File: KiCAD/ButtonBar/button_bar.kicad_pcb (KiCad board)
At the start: 2 copper layers, 14 parts, among them P1 Buttons, SW1 SW_UP, SW2 SW_DN, SW3 SW_OK, SW4 SW_LT, SW5 SW_RT, SW6 RESET

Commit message: redo tracks
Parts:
- moved R1 11.4 mm to (219.2, 85.6)
- moved R2 10.4 mm to (198.3, 58.9), turned to 180 degrees
- moved R4 5.86 mm to (198.0, 85.6), turned to 0 degrees
- moved R10 5.32 mm to (219.8, 58.8)
- moved R3 1.24 mm to (208.7, 85.6)
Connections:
- C1 pad 1: /RST -> GND
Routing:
- net /SW: track 118.9 -> 0.00 mm, vias 1 -> 0
- net /PWR: track 94.8 -> 0.00 mm
- net GND: track 73.3 -> 0.00 mm
- net N-000004: track 46.9 -> 0.00 mm
- net N-000002: track 43.0 -> 0.00 mm
- net N-000003: track 38.8 -> 0.00 mm
- net /RST: track 27.5 -> 0.00 mm
- net N-000001: track 17.8 -> 0.00 mm
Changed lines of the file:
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@@
   (general
     (links 34)
-    (no_connects 12)
-    (area 186.093599 35.6362 232.9942 120.4214)
+    (no_connects 34)
+    (area 0 0 0 0)
     (thickness 1.6)
     (drawings 0)
-    (tracks 64)
+    (tracks 0)
     (zones 0)
     (modules 14)
@@
     (pad 1 thru_hole circle (at 2.54 0 90) (size 1.524 1.524) (drill 0.889)
       (layers *.Cu *.Mask F.SilkS)
-      (net 2 /RST)
+      (net 4 GND)
     )
     (model "uControl_Libs/3D Modules/capa_2pas_5x5mm.wrl"
@@
   )
   (module RC03 (layer F.Cu)
-    (at 228.1682 92.583 180)
+    (at 219.1512 85.5726 180)
     (descr "Resistor, RC03")
     (tags R)
@@
   )
   (module RC03 (layer F.Cu)
-    (at 191.8462 50.8 90)
+    (at 198.3486 58.9407 180)
     (descr "Resistor, RC03")
     (tags R)
     (autoplace_cost180 10)
-    (fp_text reference R2 (at 0 0 90) (layer F.SilkS)
+    (fp_text reference R2 (at 0 0 180) (layer F.SilkS)
       (effects (font (size 1.016 1.016) (thickness 0.127)))
     )
-    (fp_text value 10K (at 0 1.9685 90) (layer F.SilkS)
+    (fp_text value 10K (at 0 1.9685 180) (layer F.SilkS)
       (effects (font (size 1.27 1.27) (thickness 0.1524)))
     )
@@
     (fp_line (start 2.159 0.889) (end 2.159 -0.889) (layer F.SilkS) (width 0.254))
     (fp_line (start 2.159 -0.889) (end -2.159 -0.889) (layer F.SilkS) (width 0.254))
-    (pad 2 thru_hole circle (at -3.81 0 90) (size 1.524 1.524) (drill 0.889)
+    (pad 2 thru_hole circle (at -3.81 0 180) (size 1.524 1.524) (drill 0.889)
       (layers *.Cu *.Mask F.SilkS)
       (net 8 N-000004)
     )
-    (pad 1 thru_hole circle (at 3.81 0 90) (size 1.524 1.524) (drill 0.889)
+    (pad 1 thru_hole circle (at 3.81 0 180) (size 1.524 1.524) (drill 0.889)
       (layers *.Cu *.Mask F.SilkS)
       (net 1 /PWR)
@@
   )
   (module RC03 (layer F.Cu)
-    (at 209.931 85.9536 180)
+    (at 208.7372 85.6234 180)
     (descr "Resistor, RC03")
     (tags R)
@@
   )
   (module RC03 (layer F.Cu)
-    (at 192.2526 86.5632 270)
+    (at 198.0438 85.6488)
     (descr "Resistor, RC03")
     (tags R)
     (autoplace_cost180 10)
-    (fp_text reference R4 (at 0 0 270) (layer F.SilkS)
+    (fp_text reference R4 (at -0.6096 -0.4572) (layer F.SilkS)
       (effects (font (size 1.016 1.016) (thickness 0.127)))
     )
-    (fp_text value 10K (at 0 1.9685 270) (layer F.SilkS)
+    (fp_text value 10K (at 0 1.9685) (layer F.SilkS)
       (effects (font (size 1.27 1.27) (thickness 0.1524)))
     )
@@
     (fp_line (start 2.159 0.889) (end 2.159 -0.889) (layer F.SilkS) (width 0.254))
     (fp_line (start 2.159 -0.889) (end -2.159 -0.889) (layer F.SilkS) (width 0.254))
-    (pad 2 thru_hole circle (at -3.81 0 270) (size 1.524 1.524) (drill 0.889)
+    (pad 2 thru_hole circle (at -3.81 0) (size 1.524 1.524) (drill 0.889)
       (layers *.Cu *.Mask F.SilkS)
       (net 6 N-000002)
     )
-    (pad 1 thru_hole circle (at 3.81 0 270) (size 1.524 1.524) (drill 0.889)
+    (pad 1 thru_hole circle (at 3.81 0) (size 1.524 1.524) (drill 0.889)
       (layers *.Cu *.Mask F.SilkS)
       (net 7 N-000003)
@@
   )
   (module RC03 (layer F.Cu)
-    (at 225.1202 58.801 180)
+    (at 219.7989 58.7883 180)
     (descr "Resistor, RC03")
     (tags R)
@@
     )
   )
-  (segment (start 191.8462 46.99) (end 204.9874 46.99) (width 0.254) (layer B.Cu) (net 1) (status 400000))
-  (segment (start 204.9874 46.99) (end 206.8682 45.1092) (width 0.254) (layer B.Cu) (net 1) (status 800000))
-  (segment (start 206.8682 45.1092) (end 206.8682 49.0326) (width 0.254) (layer F.Cu) (net 1))
-  (segment (start 219.6596 107.29) (end 222.9 107.29) (width 0.254) (layer F.Cu) (net 1))
-  (segment (start 217.9066 105.537) (end 219.6596 107.29) (width 0.254) (layer F.Cu) (net 1))
-  (segment (start 217.9066 60.071) (end 217.9066 105.537) (width 0.254) (layer F.Cu) (net 1))
-  (segment (start 206.8682 49.0326) (end 217.9066 60.071) (width 0.254) (layer F.Cu) (net 1))
-  (segment (start 230.6574 108.6612) (end 224.2712 108.6612) (width 0.254) (layer F.Cu) (net 1))
-  (segment (start 224.2712 108.6612) (end 222.9 107.29) (width 0.254) (layer F.Cu) (net 1))
-  (segment (start 230.6574 101.0412) (end 224.0688 101.0412) (width 0.254) (layer B.Cu) (net 2))
-  (segment (start 224.0688 101.0412) (end 222.9 102.21) (width 0.254) (layer B.Cu) (net 2))
-  (segment (start 222.9 102.21) (end 216.013 102.21) (width 0.254) (layer B.Cu) (net 2))
-  (segment (start 216.013 102.21) (end 207.2746 110.9484) (width 0.254) (layer B.Cu) (net 2))
-  (segment (start 192.6738 73.354) (end 195.378 73.354) (width 0.254) (layer F.Cu) (net 3) (status 400000))
-  (segment (start 203.918 64.814) (end 209.125 64.814) (width 0.254) (layer B.Cu) (net 3))
-  (segment (start 202.6158 66.1162) (end 203.918 64.814) (width 0.254) (layer B.Cu) (net 3))
-  (via (at 202.6158 66.1162) (size 0.889) (layers F.Cu B.Cu) (net 3))
-  (segment (start 195.378 73.354) (end 202.6158 66.1162) (width 0.254) (layer F.Cu) (net 3))
-  (segment (start 229.0466 73.354) (end 229.0466 77.1504) (width 0.254) (layer B.Cu) (net 3) (status 400000))
-  (segment (start 224.3582 81.8388) (end 224.3582 92.583) (width 0.254) (layer B.Cu) (net 3) (status 800000))
-  (segment (start 229.0466 77.1504) (end 224.3582 81.8388) (width 0.254) (layer B.Cu) (net 3))
-  (segment (start 211.165 73.354) (end 211.165 81.5192) (width 0.254) (layer B.Cu) (net 3) (status 400000))
-  (segment (start 209.6516 94.195) (end 210.9618 95.5052) (width 0.254) (layer B.Cu) (net 3) (status 800000))
-  (segment (start 209.6516 83.0326) (end 209.6516 94.195) (width 0.254) (layer B.Cu) (net 3))
-  (segment (start 211.165 81.5192) (end 209.6516 83.0326) (width 0.254) (layer B.Cu) (net 3))
-  (segment (start 211.3682 45.1092) (end 211.3682 55.0524) (width 0.254) (layer B.Cu) (net 3) (status 400000))
-  (segment (start 208.8896 64.5786) (end 209.125 64.814) (width 0.254) (layer B.Cu) (net 3))
-  (segment (start 209.125 64.814) (end 211.165 66.854) (width 0.254) (layer B.Cu) (net 3) (status 800000))
-  (segment (start 208.8896 57.531) (end 208.8896 64.5786) (width 0.254) (layer B.Cu) (net 3))
-  (segment (start 211.3682 55.0524) (end 208.8896 57.531) (width 0.254) (layer B.Cu) (net 3))
-  (segment (start 224.3582 92.583) (end 224.3582 99.822) (width 0.254) (layer F.Cu) (net 3))
-  (segment (start 224.3582 99.822) (end 230.6574 106.1212) (width 0.254) (layer F.Cu) (net 3))
-  (segment (start 224.3582 92.583) (end 213.884 92.583) (width 0.254) (layer B.Cu) (net 3))
-  (segment (start 213.884 92.583) (end 210.9618 95.5052) (width 0.254) (layer B.Cu) (net 3))
-  (segment (start 231.9782 92.583) (end 231.9782 61.849) (width 0.254) (layer B.Cu) (net 4) (status 400000))
-  (segment (start 231.9782 61.849) (end 228.9302 58.801) (width 0.254) (layer B.Cu) (net 4) (status 800000))
-  (segment (start 230.6574 103.5812) (end 232.4862 103.5812) (width 0.254) (layer B.Cu) (net 4) (status 400000))
-  (segment (start 233.0958 93.7006) (end 231.9782 92.583) (width 0.254) (layer B.Cu) (net 4) (status 800000))
-  (segment (start 233.0958 102.9716) (end 233.0958 93.7006) (width 0.254) (layer B.Cu) (net 4))
-  (segment (start 232.4862 103.5812) (end 233.0958 102.9716) (width 0.254) (layer B.Cu) (net 4))
-  (segment (start 230.6574 103.5812) (end 230.6574 103.7082) (width 0.254) (layer B.Cu) (net 4))
-  (segment (start 216.9172 117.4484) (end 211.7746 117.4484) (width 0.254) (layer B.Cu) (net 4))
-  (segment (start 230.6574 103.7082) (end 216.9172 117.4484) (width 0.254) (layer B.Cu) (net 4))
-  (segment (start 221.3102 58.801) (end 221.3102 63.6176) (width 0.254) (layer B.Cu) (net 5) (status 400000))
-  (segment (start 221.3102 63.6176) (end 224.5466 66.854) (width 0.254) (layer B.Cu) (net 5) (status 800000))
-  (segment (start 212.9282 58.928) (end 221.1832 58.928) (width 0.254) (layer B.Cu) (net 5) (status C00000))
-  (segment (start 221.1832 58.928) (end 221.3102 58.801) (width 0.254) (layer B.Cu) (net 5) (status C00000))
-  (segment (start 188.1738 73.354) (end 188.1738 78.6744) (width 0.254) (layer B.Cu) (net 6) (status 400000))
-  (segment (start 188.1738 78.6744) (end 192.2526 82.7532) (width 0.254) (layer B.Cu) (net 6) (status 800000))
-  (segment (start 205.3082 58.928) (end 195.326 58.928) (width 0.254) (layer F.Cu) (net 6) (status 400000))
-  (segment (start 188.1738 66.0802) (end 188.1738 66.854) (width 0.254) (layer F.Cu) (net 6) (status C00000))
-  (segment (start 195.326 58.928) (end 188.1738 66.0802) (width 0.254) (layer F.Cu) (net 6) (status 800000))
-  (segment (start 188.1738 73.354) (end 188.1738 77.5822) (width 0.254) (layer B.Cu) (net 6) (status 400000))
-  (segment (start 188.1738 77.5822) (end 192.9638 82.3722) (width 0.254) (layer B.Cu) (net 6))
-  (segment (start 213.741 85.9536) (end 213.741 80.43) (width 0.254) (layer F.Cu) (net 7) (status 400000))
-  (segment (start 213.741 80.43) (end 206.665 73.354) (width 0.254) (layer F.Cu) (net 7) (status 800000))
-  (segment (start 192.2526 90.3732) (end 209.3214 90.3732) (width 0.254) (layer F.Cu) (net 7) (status 400000))
-  (segment (start 209.3214 90.3732) (end 213.741 85.9536) (width 0.254) (layer F.Cu) (net 7) (status 800000))
-  (segment (start 206.121 85.9536) (end 206.121 82.55) (width 0.254) (layer B.Cu) (net 8) (status 400000))
-  (segment (start 198.9582 61.722) (end 191.8462 54.61) (width 0.254) (layer B.Cu) (net 8) (status 800000))
-  (segment (start 198.9582 75.3872) (end 198.9582 61.722) (width 0.254) (layer B.Cu) (net 8))
-  (segment (start 206.121 82.55) (end 198.9582 75.3872) (width 0.254) (layer B.Cu) (net 8))
-  (segment (start 206.4618 95.5052) (end 206.4618 86.2944) (width 0.254) (layer B.Cu) (net 8))
-  (segment (start 206.4618 86.2944) (end 206.121 85.9536) (width 0.254) (layer B.Cu) (net 8))
 )

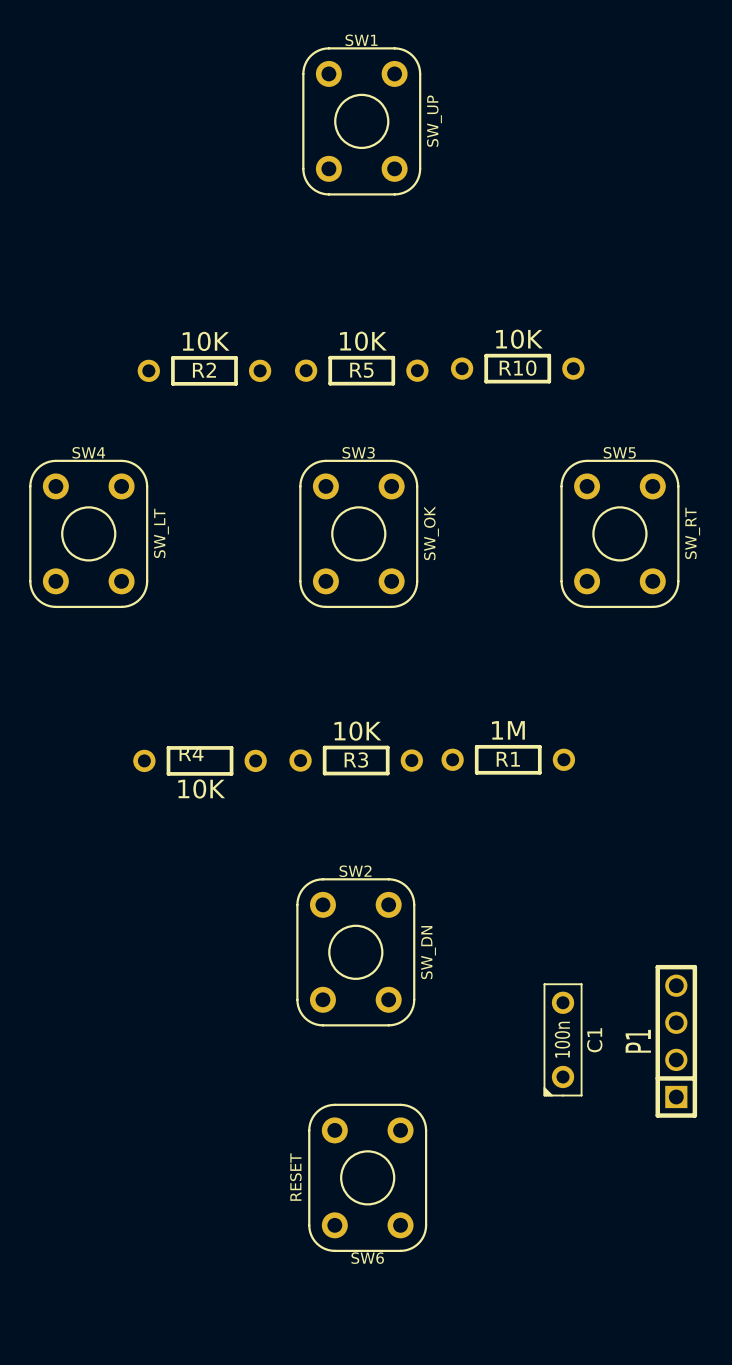
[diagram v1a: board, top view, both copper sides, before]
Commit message: finished tracks on ButtonBar
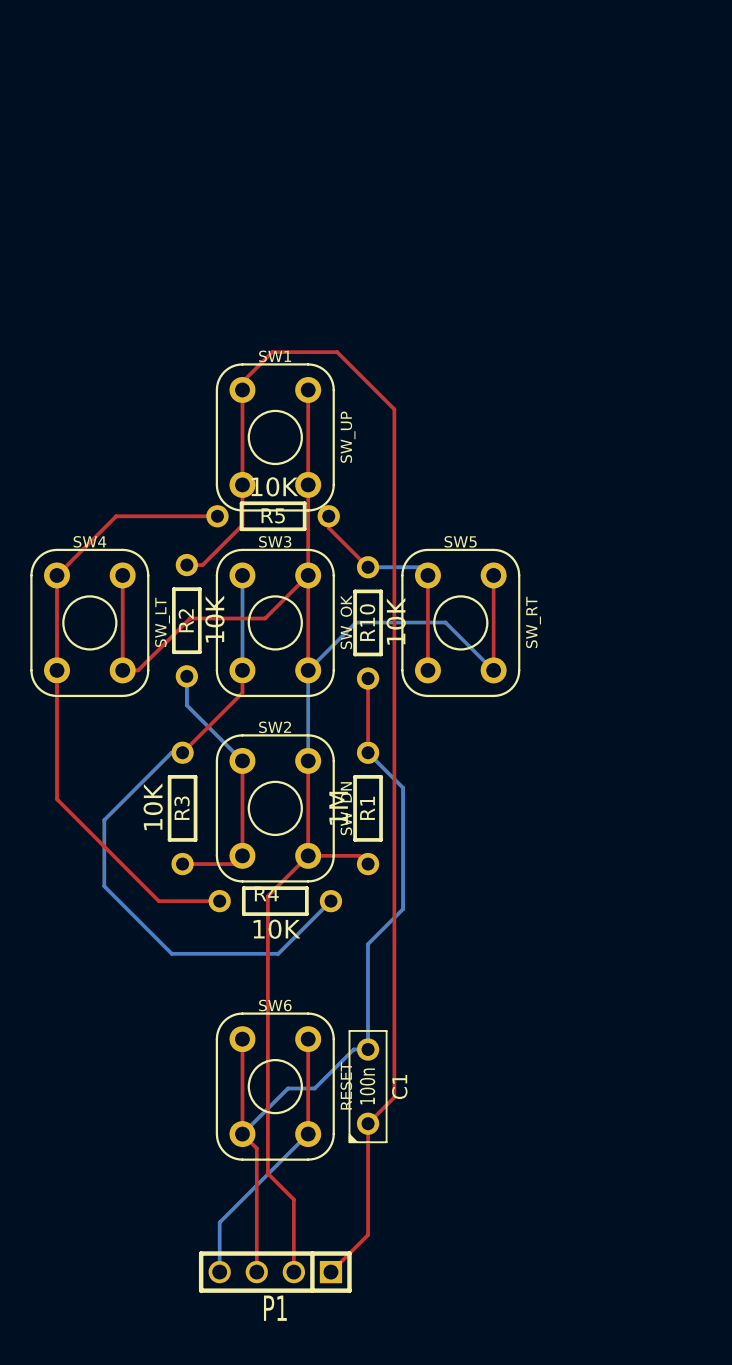
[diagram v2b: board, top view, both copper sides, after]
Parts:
- moved P1 31.7 mm to (203.2, 120.7), turned to 180 degrees
- moved SW1 22.4 mm to (203.2, 63.5)
- moved R10 20.2 mm to (209.6, 76.2), turned to 90 degrees
- moved R2 17.1 mm to (197.1, 76.0), turned to 90 degrees
- moved C1 13.7 mm to (209.6, 108.0)
- moved SW5 12.5 mm to (215.9, 76.2)
- moved R3 12.3 mm to (196.8, 88.9), turned to 270 degrees
- moved R5 11.7 mm to (203.0, 68.9)
- moved SW2 11.3 mm to (203.2, 88.9)
- moved R4 10.9 mm to (203.2, 95.2)
- moved R1 10.2 mm to (209.6, 88.9), turned to 270 degrees
- moved SW6 8.89 mm to (203.2, 108.0), turned to 0 degrees
- moved SW3 8.36 mm to (203.2, 76.2)
- moved SW4 6.10 mm to (190.5, 76.2)
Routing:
- net /SW: track 0.00 -> 110.4 mm
- net /PWR: track 0.00 -> 88.5 mm
- net GND: track 0.00 -> 54.7 mm
- net N-000003: track 0.00 -> 44.6 mm
- net N-000002: track 0.00 -> 42.0 mm
- net /RST: track 0.00 -> 18.5 mm
- net N-000004: track 0.00 -> 18.2 mm
- net N-000001: track 0.00 -> 15.4 mm

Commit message: button board pcb update ajm
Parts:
- added H1: CONN_1, vite_3mm, F.Cu at (190.5, 63.5)
- added H2: CONN_1, vite_3mm, F.Cu at (215.9, 63.5)
- added H3: CONN_1, vite_3mm, F.Cu at (215.9, 108.0)
- added H4: CONN_1, vite_3mm, F.Cu at (190.5, 108.0)
- moved R3 25.4 mm to (196.8, 63.5), turned to 90 degrees
- moved R4 20.1 mm to (196.8, 76.2), turned to 90 degrees
- moved R2 17.6 mm to (209.6, 63.5), turned to 270 degrees
- moved R1 12.7 mm to (196.8, 88.9), turned to 90 degrees
- moved R6 12.7 mm to (209.6, 88.9)
- moved R5 9.78 mm to (209.6, 76.2), turned to 270 degrees
- moved C1 9.35 mm to (203.2, 101.1), turned to 180 degrees
- moved P1 3.81 mm to (203.2, 116.8)
- turned SW2 to 180 degrees
- turned SW4 to 180 degrees
- renumbered R10 to R6
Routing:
- net N-000004: track 18.2 -> 69.2 mm
- net N-000001: track 44.6 -> 15.9 mm
- net N-000003: track 42.0 -> 25.1 mm
- net /PWR: track 88.5 -> 76.3 mm
- net /SW: track 110.4 -> 121.9 mm
- net GND: track 54.7 -> 44.6 mm
- net N-000002: track 15.4 -> 19.9 mm
- net /RST: track 18.5 -> 17.1 mm
- added copper zone on B.Cu, net GND
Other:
- board outline added: 38.1 x 63.5 mm

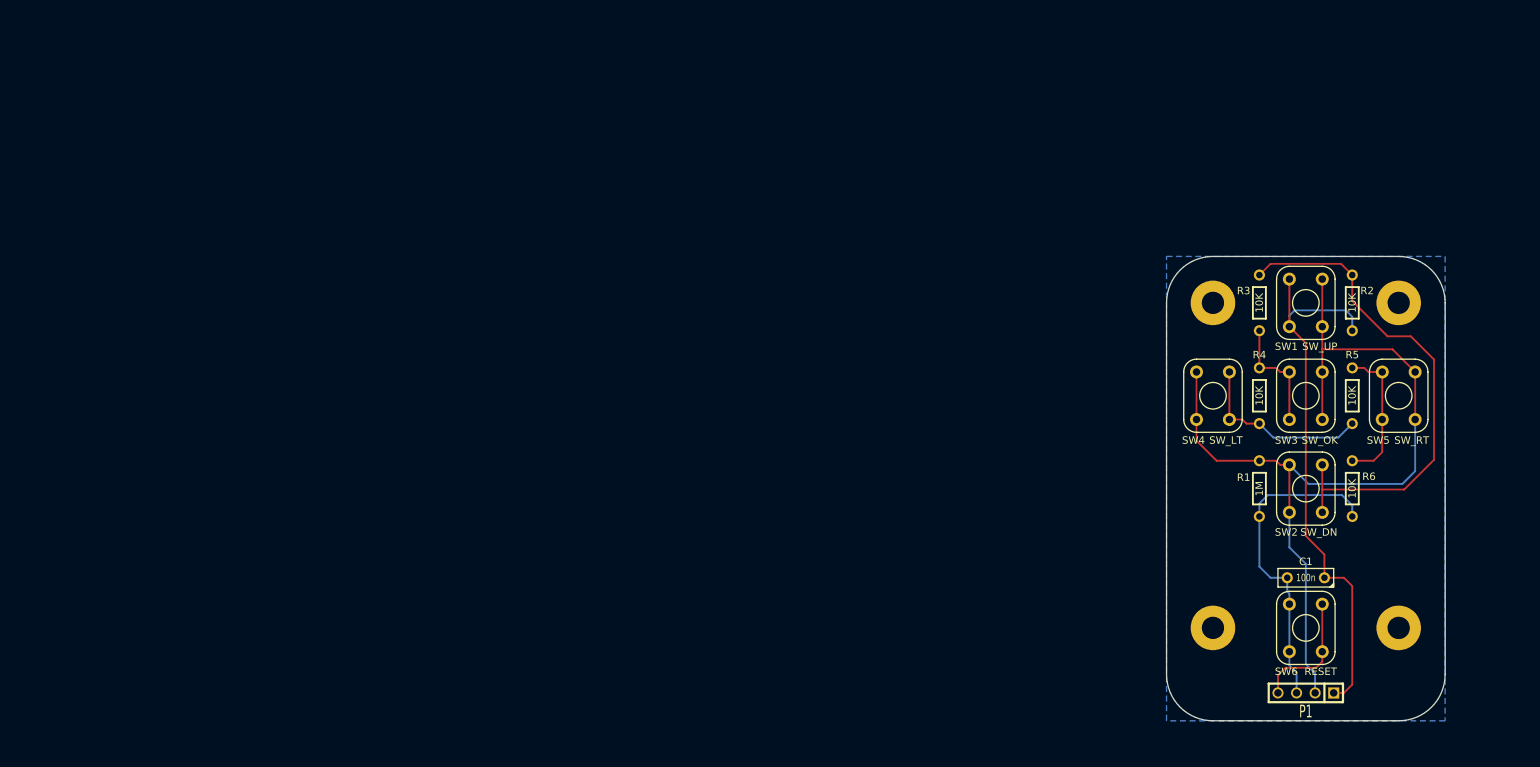
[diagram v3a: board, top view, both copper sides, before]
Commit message: added KiCad design files for TiNA
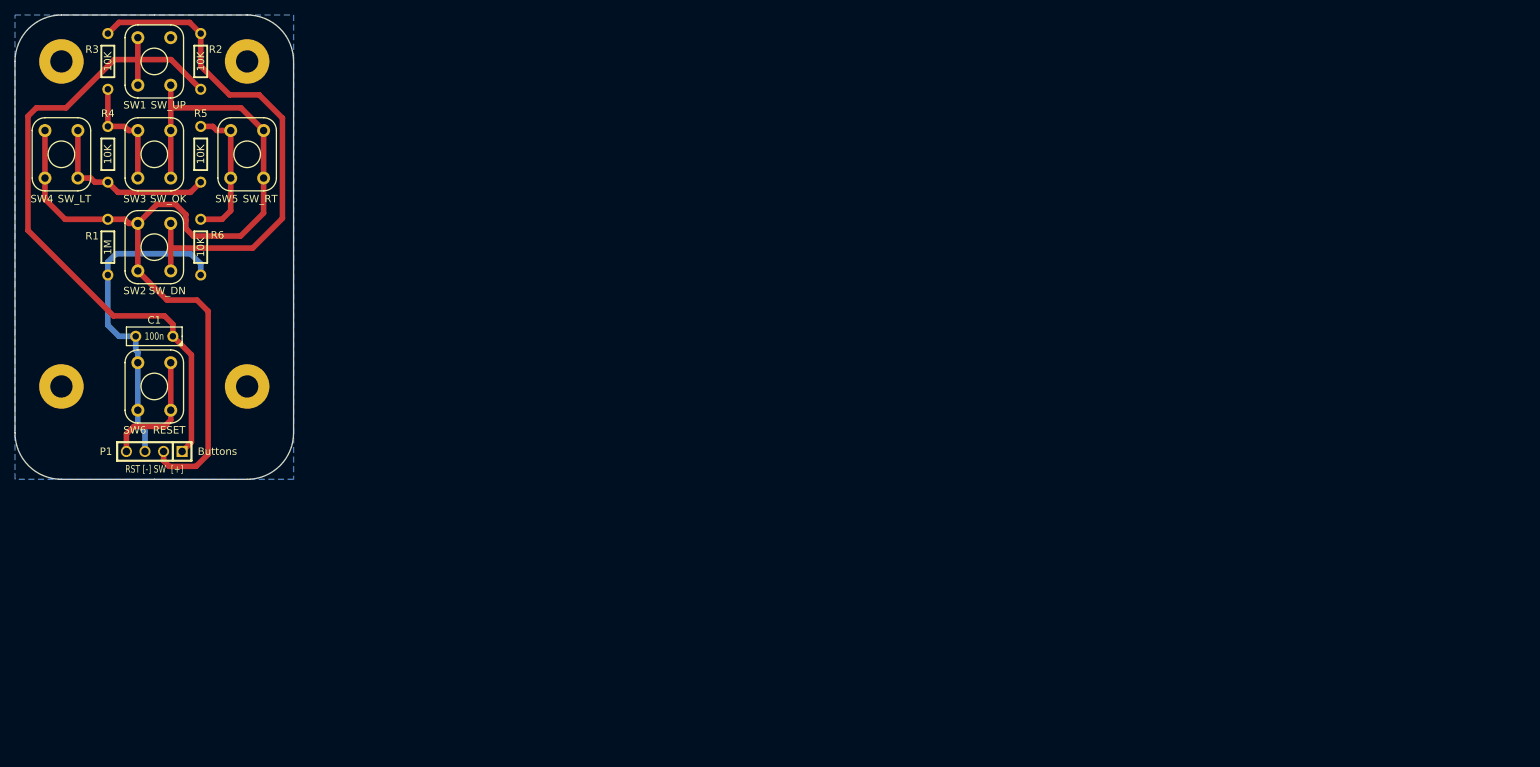
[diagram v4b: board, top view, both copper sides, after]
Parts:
- moved H2 160.9 mm to (58.4, 30.5)
- moved H3 160.9 mm to (58.4, 74.9)
- moved R2 160.9 mm to (52.1, 30.5)
- moved R5 160.9 mm to (52.1, 43.2)
- moved R6 160.9 mm to (52.1, 55.9)
- moved SW5 160.9 mm to (58.4, 43.2)
- moved C1 160.9 mm to (45.7, 68.1)
- moved H1 160.9 mm to (33.0, 30.5)
- moved H4 160.9 mm to (33.0, 74.9)
- moved P1 160.9 mm to (45.7, 83.8)
- moved R1 160.9 mm to (39.4, 55.9)
- moved R3 160.9 mm to (39.4, 30.5)
- moved R4 160.9 mm to (39.4, 43.2)
- moved SW1 160.9 mm to (45.7, 30.5)
- moved SW2 160.9 mm to (45.7, 55.9)
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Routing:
- net /PWR: track 76.3 -> 94.8 mm
- net /SW: track 121.9 -> 130.2 mm
- net N-000004: track 69.2 -> 69.7 mm
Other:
- outline, holes or cut-outs redrawn
- net class 20mil added: clearance 0.254, trace_width 0.508, via_dia 0.889, via_drill 0.635
- net class 30mil added: clearance 0.254, trace_width 0.762, via_dia 0.889, via_drill 0.635
- board text added: "RST [-] SW [+]"
